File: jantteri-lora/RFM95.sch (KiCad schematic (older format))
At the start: 3 parts

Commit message: Lora PCB desging
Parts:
- added C3: 100n, Capacitor_SMD:C_0603_1608Metric, symbol Device:C_Small
- gave numbers to parts that had none: 3
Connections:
- net 3V3: now also C3.1
- net GND: now also C3.2
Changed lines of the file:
@@
 $Descr A4 11693 8268
 encoding utf-8
-Sheet 7 7
+Sheet 4 8
 Title ""
 Date ""
@@
 $EndDescr
 $Comp
-L RF_Module:RFM95W-868S2 U?
+L RF_Module:RFM95W-868S2 U3
 U 1 1 60128928
 P 6250 3450
-F 0 "U?" H 5550 4050 50  0000 C CNN
+F 0 "U3" H 5550 4050 50  0000 C CNN
 F 1 "RFM95W-868S2" H 5800 3950 50  0000 C CNN
 F 2 "RF_Module:HOPERF_RFM9XW_SMD" H 2950 5100 50  0001 C CNN
@@
 	6250 4100 6250 4150
 $Comp
-L Connector:Conn_01x01_Male J?
+L Connector:Conn_01x01_Male J1
 U 1 1 602449E3
 P 7100 3150
-F 0 "J?" H 7200 2950 50  0000 R CNN
+F 0 "J1" H 7200 2950 50  0000 R CNN
 F 1 "ANT" H 7250 3050 50  0000 R CNN
 F 2 "Connector_PinHeader_2.54mm:PinHeader_1x01_P2.54mm_Vertical" H 7100 3150 50  0001 C CNN
@@
 AR Path="/611406BB" Ref="C?"  Part="1"
 AR Path="/6116447D/611406BB" Ref="C?"  Part="1"
-F 0 "C?" H 4892 3496 50  0000 L CNN
+AR Path="/6112EDA0/611406BB" Ref="C4"  Part="1"
+F 0 "C4" H 4892 3496 50  0000 L CNN
 F 1 "100n" H 4892 3405 50  0000 L CNN
 F 2 "Capacitor_SMD:C_0603_1608Metric" H 4800 3450 50  0001 C CNN
@@
 Text HLabel 4800 3550 3    50   Input ~ 0
 GND
+$Comp
+L Device:C_Small C?
+U 1 1 611BC88F
+P 4450 3450
+AR Path="/611BC88F" Ref="C?"  Part="1"
+AR Path="/6116447D/611BC88F" Ref="C?"  Part="1"
+AR Path="/6112EDA0/611BC88F" Ref="C3"  Part="1"
+F 0 "C3" H 4542 3496 50  0000 L CNN
+F 1 "100n" H 4542 3405 50  0000 L CNN
+F 2 "Capacitor_SMD:C_0603_1608Metric" H 4450 3450 50  0001 C CNN
+F 3 "~" H 4450 3450 50  0001 C CNN
+F 4 "C14663" H 4450 3450 50  0001 C CNN "LCSC"
+	1    4450 3450
+	1    0    0    -1
+$EndComp
+Wire Wire Line
+	4450 3350 4800 3350
+Wire Wire Line
+	4450 3550 4800 3550
 $EndSCHEMATC

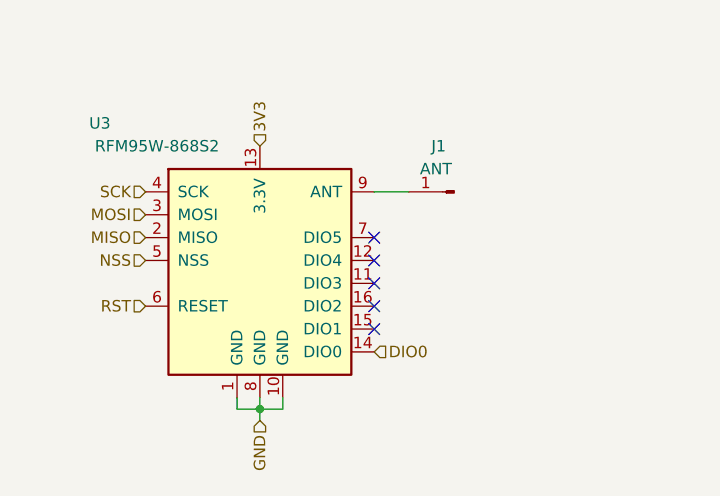
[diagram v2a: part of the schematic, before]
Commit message: Tuubijantteri design Ordered
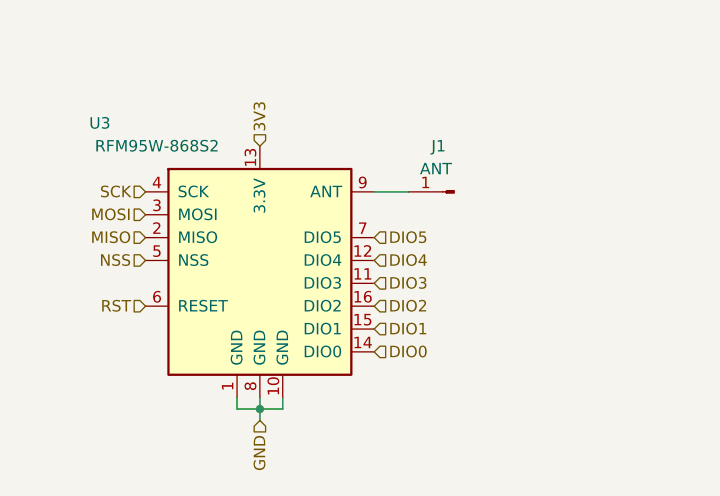
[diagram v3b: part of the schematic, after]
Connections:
- net DIO3: now reaches U3.11 (DIO3)
- net DIO4: now reaches U3.12 (DIO4)
- net DIO1: now reaches U3.15 (DIO1)
- net DIO2: now reaches U3.16 (DIO2)
- net DIO5: now reaches U3.7 (DIO5)
- no-connect marks 5 -> 0
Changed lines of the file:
@@
 $Descr A4 11693 8268
 encoding utf-8
-Sheet 3 8
+Sheet 3 6
 Title ""
 Date ""
@@
 Comment4 ""
 $EndDescr
-$Comp
-L RF_Module:RFM95W-868S2 U3
-U 1 1 60128928
-P 6250 3450
-F 0 "U3" H 5550 4050 50  0000 C CNN
-F 1 "RFM95W-868S2" H 5800 3950 50  0000 C CNN
-F 2 "RF_Module:HOPERF_RFM9XW_SMD" H 2950 5100 50  0001 C CNN
-F 3 "https://www.hoperf.com/data/upload/portal/20181127/5bfcbea20e9ef.pdf" H 2950 5100 50  0001 C CNN
-	1    6250 3450
-	1    0    0    -1
-$EndComp
 Wire Wire Line
 	6150 4050 6150 4100
@@
 Wire Wire Line
 	6750 3150 6900 3150
-NoConn ~ 6750 3750
-NoConn ~ 6750 3650
-NoConn ~ 6750 3550
-NoConn ~ 6750 3450
-NoConn ~ 6750 3350
 Text Notes 7900 600  0    50   ~ 0
 RFM95\n
@@
 Wire Wire Line
 	4450 3550 4800 3550
+Text HLabel 6750 3750 2    50   Input ~ 0
+DIO1
+Text HLabel 6750 3650 2    50   Input ~ 0
+DIO2
+Text HLabel 6750 3550 2    50   Input ~ 0
+DIO3
+Text HLabel 6750 3450 2    50   Input ~ 0
+DIO4
+Text HLabel 6750 3350 2    50   Input ~ 0
+DIO5
+$Comp
+L RF_Module:RFM95W-868S2 U3
+U 1 1 60128928
+P 6250 3450
+F 0 "U3" H 5550 4050 50  0000 C CNN
+F 1 "RFM95W-868S2" H 5800 3950 50  0000 C CNN
+F 2 "RF_Module:HOPERF_RFM9XW_SMD" H 2950 5100 50  0001 C CNN
+F 3 "https://www.hoperf.com/data/upload/portal/20181127/5bfcbea20e9ef.pdf" H 2950 5100 50  0001 C CNN
+	1    6250 3450
+	1    0    0    -1
+$EndComp
 $EndSCHEMATC
